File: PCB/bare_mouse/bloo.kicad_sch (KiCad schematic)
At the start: 105 parts, among them J1 Serial Debug Header, J10 Conn_01x06_Female, J2 SWD Header, J4 Conn_ARM_JTAG_SWD_10, J5 SWD Header, M1 M1_Conn_Alt, M2 M2_Conn_Alt, Q0 TEFT4300, Q1 TEFT4300, Q10 Q_NMOS_GSD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

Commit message: Reviewed and updated schematics accordingly, updated BOM, created PCB Design Notes
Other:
- note added: "Bidirect."
- note added: "INPUT_NET"
- note added: "IO_NET"
- note added: "Input"
- note added: "Key"
- note added: "OUTPUT_NET"
- note added: "Output"
- note added: "only correctly labelled for bluepill"

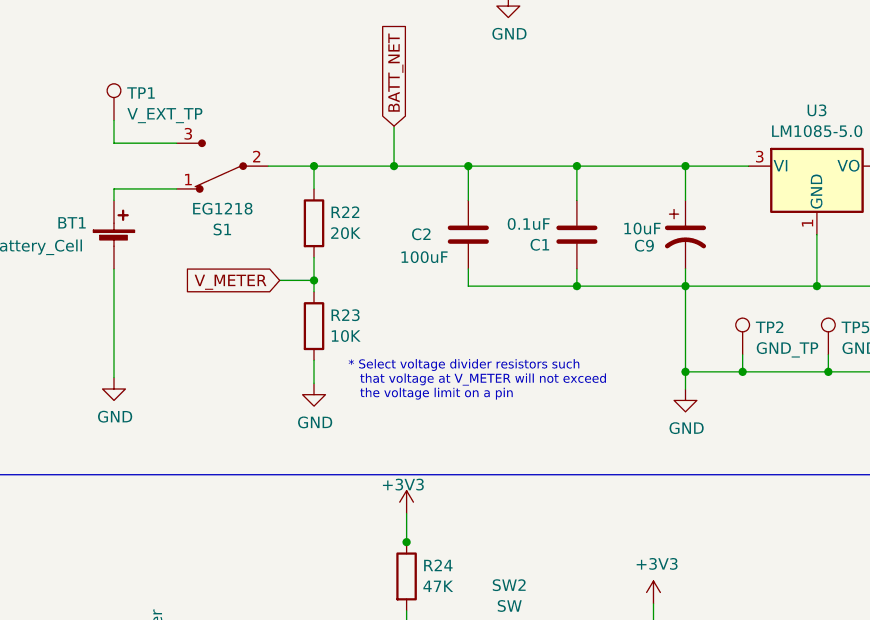
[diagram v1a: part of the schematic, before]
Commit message: Completed routing for version using bluepill, no DRC errors. Began routing for version with no bluepill
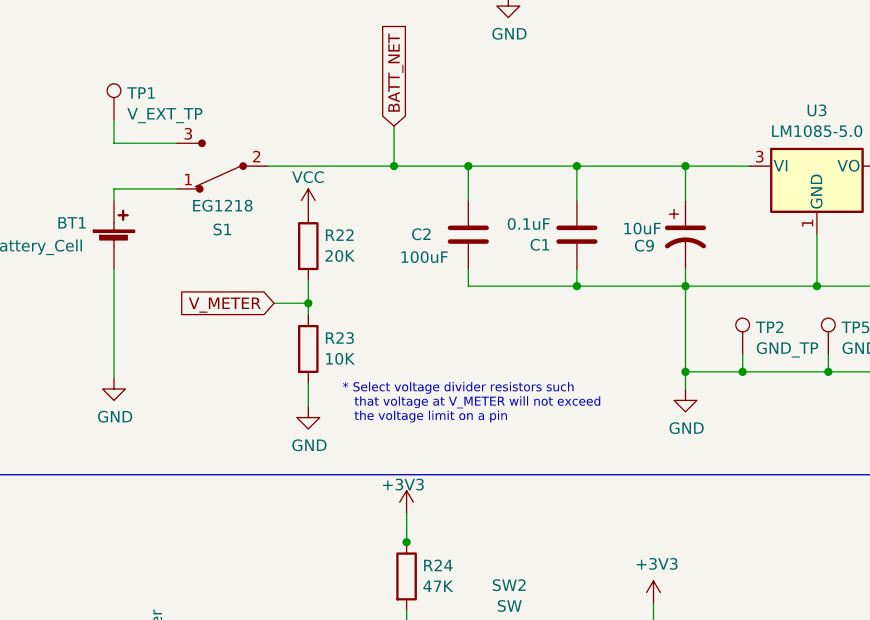
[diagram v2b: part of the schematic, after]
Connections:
- net BATT_NET: no longer R22.1
- net VCC: now also R22.1
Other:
- moved on the sheet: R22, R23
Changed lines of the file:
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@@
   (junction (at 342.265 205.105) (diameter 0) (color 0 0 0 0)
   )
-  (junction (at 51.435 182.245) (diameter 0) (color 0 0 0 0)
+  (junction (at 50.8 184.785) (diameter 0) (color 0 0 0 0)
   )
   (junction (at 92.71 182.88) (diameter 0) (color 0 0 0 0)
@@
   (junction (at 116.205 136.525) (diameter 0) (color 0 0 0 0)
   )
-  (junction (at 51.435 169.545) (diameter 0) (color 0 0 0 0)
-  )
   (junction (at 104.267 110.363) (diameter 0) (color 0 0 0 0)
   )
@@
     (stroke (width 0) (type default))
   )
-  (wire (pts (xy 51.435 182.245) (xy 51.435 183.515))
+  (wire (pts (xy 50.8 184.785) (xy 50.8 186.055))
     (stroke (width 0) (type default))
   )
@@
     (stroke (width 0) (type default))
   )
-  (wire (pts (xy 51.435 169.545) (xy 60.325 169.545))
+  (wire (pts (xy 46.355 169.545) (xy 60.325 169.545))
     (stroke (width 0) (type default))
   )
@@
     (stroke (width 0) (type default))
   )
-  (wire (pts (xy 51.435 182.245) (xy 47.625 182.245))
+  (wire (pts (xy 50.8 184.785) (xy 46.99 184.785))
     (stroke (width 0) (type default))
   )
@@
     (stroke (width 0) (type default))
   )
-  (wire (pts (xy 46.355 169.545) (xy 51.435 169.545))
-    (stroke (width 0) (type default))
-  )
   (wire (pts (xy 60.198 106.553) (xy 60.198 110.363))
     (stroke (width 0) (type default))
@@
     (stroke (width 0) (type default))
   )
-  (wire (pts (xy 51.435 179.705) (xy 51.435 182.245))
+  (wire (pts (xy 50.8 182.245) (xy 50.8 184.785))
     (stroke (width 0) (type default))
   )
@@
     (stroke (width 0) (type default))
   )
-  (wire (pts (xy 51.435 191.135) (xy 51.435 193.675))
+  (wire (pts (xy 50.8 193.675) (xy 50.8 196.215))
     (stroke (width 0) (type default))
   )
@@
     (stroke (width 0) (type default))
   )
-  (wire (pts (xy 51.435 172.085) (xy 51.435 169.545))
-    (stroke (width 0) (type default))
-  )
   (wire (pts (xy 149.733 48.895) (xy 136.398 48.895))
     (stroke (width 0) (type default))
@@
   )
   (text "* Select voltage divider resistors such\n   that voltage at V_METER will not exceed\n   the voltage limit on a pin"
-    (at 55.245 195.58 0)
+    (at 54.61 198.12 0)
     (effects (font (size 0.9906 0.9906)) (justify left bottom))
   )
@@
     )
   )
-  (global_label "V_METER" (shape input) (at 47.625 182.245 180) (fields_autoplaced)
+  (global_label "V_METER" (shape input) (at 46.99 184.785 180) (fields_autoplaced)
     (effects (font (size 1.27 1.27)) (justify right))
-    (property "Intersheetrefs" "${INTERSHEET_REFS}" (at 37.2508 182.245 0)
+    (property "Intersheetrefs" "${INTERSHEET_REFS}" (at 36.6158 184.785 0)
       (effects (font (size 1.27 1.27)) (justify right) hide)
     )
@@
       (effects (font (size 1.27 1.27)))
     )
-    (property "Value" "EG1218" (at 41.275 174.3202 0)
+    (property "Value" "EG1218" (at 41.275 173.99 0)
       (effects (font (size 1.27 1.27)))
     )
@@
     )
   )
-  (symbol (lib_id "Device:R") (at 51.435 175.895 0) (unit 1)
+  (symbol (lib_id "Device:R") (at 50.8 178.435 0) (unit 1)
     (in_bom yes) (on_board yes) (dnp no)
-    (property "Reference" "R22" (at 53.213 174.7266 0)
+    (property "Reference" "R22" (at 52.578 177.2666 0)
       (effects (font (size 1.27 1.27)) (justify left))
     )
-    (property "Value" "20K" (at 53.213 177.038 0)
+    (property "Value" "20K" (at 52.578 179.578 0)
       (effects (font (size 1.27 1.27)) (justify left))
     )
-    (property "Footprint" "Resistor_SMD:R_1206_3216Metric_Pad1.30x1.75mm_HandSolder" (at 49.657 175.895 90)
+    (property "Footprint" "Resistor_SMD:R_1206_3216Metric_Pad1.30x1.75mm_HandSolder" (at 49.022 178.435 90)
       (effects (font (size 1.27 1.27)) hide)
     )
-    (property "Datasheet" "~" (at 51.435 175.895 0)
+    (property "Datasheet" "~" (at 50.8 178.435 0)
       (effects (font (size 1.27 1.27)) hide)
     )
@@
     )
   )
-  (symbol (lib_id "Device:R") (at 51.435 187.325 0) (unit 1)
+  (symbol (lib_id "Device:R") (at 50.8 189.865 0) (unit 1)
     (in_bom yes) (on_board yes) (dnp no)
-    (property "Reference" "R23" (at 53.213 186.1566 0)
+    (property "Reference" "R23" (at 52.578 188.6966 0)
       (effects (font (size 1.27 1.27)) (justify left))
     )
-    (property "Value" "10K" (at 53.213 188.468 0)
+    (property "Value" "10K" (at 52.578 191.008 0)
       (effects (font (size 1.27 1.27)) (justify left))
     )
-    (property "Footprint" "Resistor_SMD:R_1206_3216Metric_Pad1.30x1.75mm_HandSolder" (at 49.657 187.325 90)
+    (property "Footprint" "Resistor_SMD:R_1206_3216Metric_Pad1.30x1.75mm_HandSolder" (at 49.022 189.865 90)
       (effects (font (size 1.27 1.27)) hide)
     )
-    (property "Datasheet" "~" (at 51.435 187.325 0)
+    (property "Datasheet" "~" (at 50.8 189.865 0)
       (effects (font (size 1.27 1.27)) hide)
     )
@@
     )
   )
-  (symbol (lib_id "power:GND") (at 51.435 193.675 0) (unit 1)
+  (symbol (lib_id "power:GND") (at 50.8 196.215 0) (unit 1)
     (in_bom yes) (on_board yes) (dnp no)
-    (property "Reference" "#PWR0114" (at 51.435 200.025 0)
+    (property "Reference" "#PWR0114" (at 50.8 202.565 0)
       (effects (font (size 1.27 1.27)) hide)
     )
-    (property "Value" "GND" (at 51.562 198.0692 0)
+    (property "Value" "GND" (at 50.927 200.6092 0)
       (effects (font (size 1.27 1.27)))
     )
-    (property "Footprint" "" (at 51.435 193.675 0)
+    (property "Footprint" "" (at 50.8 196.215 0)
       (effects (font (size 1.27 1.27)) hide)
     )
-    (property "Datasheet" "" (at 51.435 193.675 0)
+    (property "Datasheet" "" (at 50.8 196.215 0)
       (effects (font (size 1.27 1.27)) hide)
     )
@@
         )
       )
+    )
+  )
+  (symbol (lib_id "power:VCC") (at 50.8 174.625 0) (unit 1)
+    (in_bom yes) (on_board yes) (dnp no)
+    (property "Reference" "#PWR020" (at 50.8 178.435 0)
+      (effects (font (size 1.27 1.27)) hide)
+    )
+    (property "Value" "VCC" (at 50.8 170.815 0)
+      (effects (font (size 1.27 1.27)))
+    )
+    (property "Footprint" "" (at 50.8 174.625 0)
+      (effects (font (size 1.27 1.27)) hide)
+    )
+    (property "Datasheet" "" (at 50.8 174.625 0)
+      (effects (font (size 1.27 1.27)) hide)
+    )
+    (pin "1")
+    (instances
+      (project "bloo"
+        (path "/9031bb33-c6aa-4758-bf5c-3274ed3ebab7"
+          (reference "#PWR020") (unit 1)
+        )
+      )

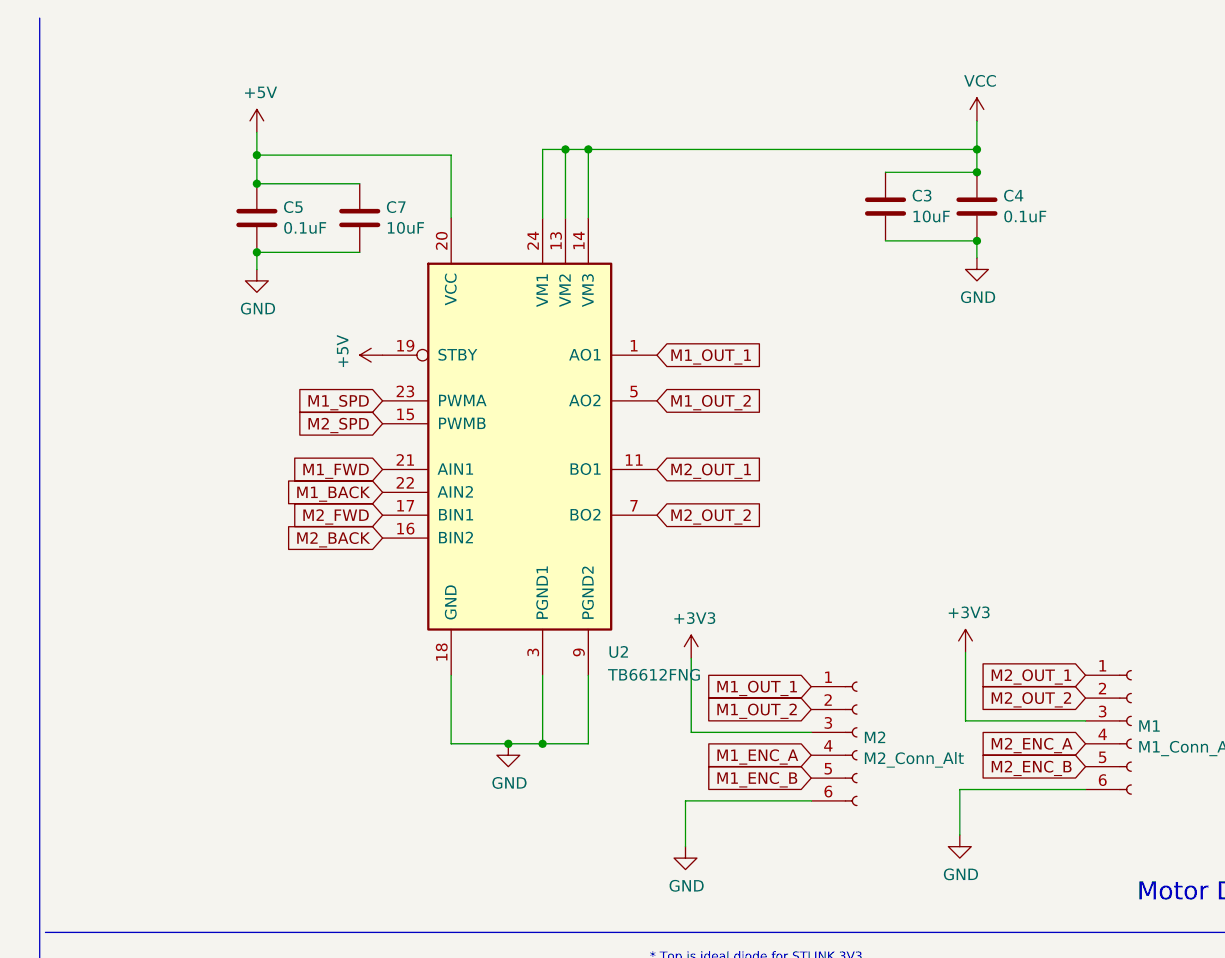
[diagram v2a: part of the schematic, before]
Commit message: Updated bluepill version of mouse to use L293D motor driver rather than TB6612FNG
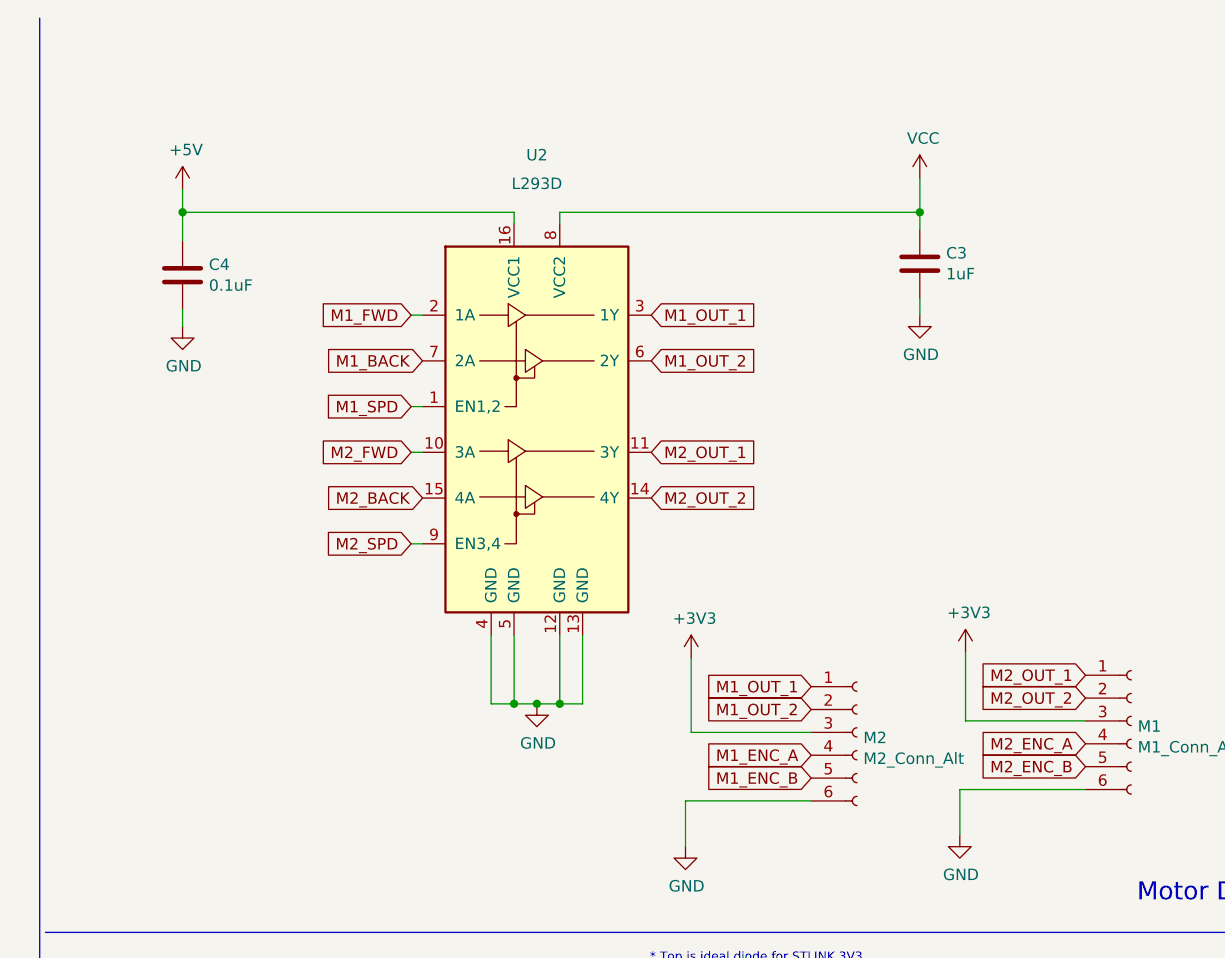
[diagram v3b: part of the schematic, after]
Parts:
- removed C5: 0.1uF, Capacitor_SMD:C_1206_3216Metric_Pad1.33x1.80mm_HandSolder, symbol Device:C
- removed C7: 10uF, Capacitor_SMD:C_1206_3216Metric_Pad1.33x1.80mm_HandSolder, symbol Device:C
- removed U2: TB6612FNG, Package_SO:SSOP-24_5.3x8.2mm_P0.65mm, symbol Driver_Motor:TB6612FNG
- added U2: L293D, Package_DIP:DIP-16_W7.62mm, symbol Driver_Motor:L293D
- C3: value 10uF -> 1uF
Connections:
- net +5V: now also C4.1, U2.16 (VCC1)
- net GND: now also U2.12 (GND), U2.13 (GND), U2.4 (GND), U2.5 (GND)
- net M1_BACK: now also U2.7 (2A)
- net M1_FWD: now also U2.2 (1A)
- net M1_OUT_1: now also U2.3 (1Y)
- net M1_OUT_2: now also U2.6 (2Y)
- net M1_SPD: now also U2.1 (EN1,2)
- net M2_BACK: now also U2.15 (4A)
- net M2_FWD: now also U2.10 (3A)
- net M2_OUT_1: now also U2.11 (3Y)
- net M2_OUT_2: now also U2.14 (4Y)
- net M2_SPD: now also U2.9 (EN3,4)
- net VCC: now also U2.8 (VCC2); no longer C4.1
